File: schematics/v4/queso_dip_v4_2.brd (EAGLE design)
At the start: 41 x 50 mm, 45 parts, among them Q1 FOXSDLF/120-20, U1 PRTR5V0U2X,215, U2 PRTR5V0U2X,215, U3 PRTR5V0U2X,215, U4 PRTR5V0U2X,215, U5 PRTR5V0U2X,215, X1 USB-A-HU, X2 USB-A-HU, X3 USB-A-HU, X4 USB-A-HU

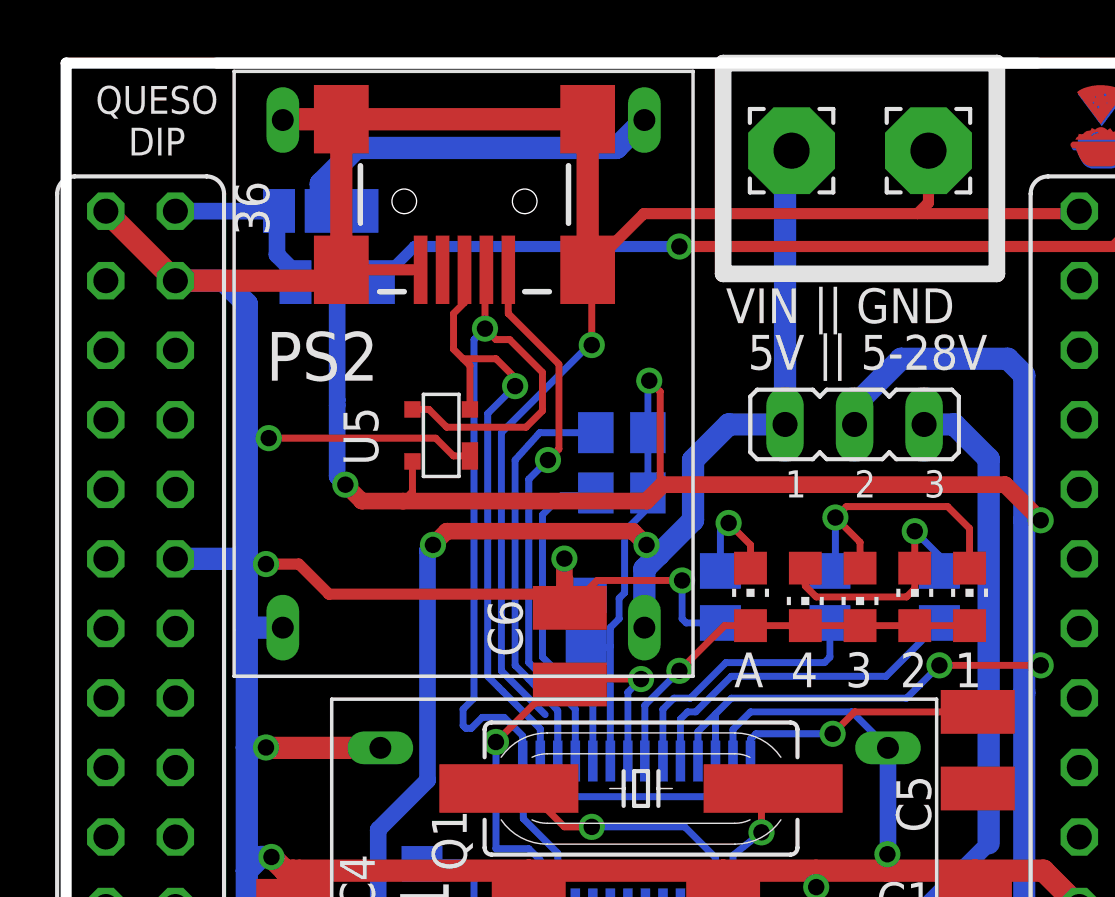
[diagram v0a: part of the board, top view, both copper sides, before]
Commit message: fixed micro usb
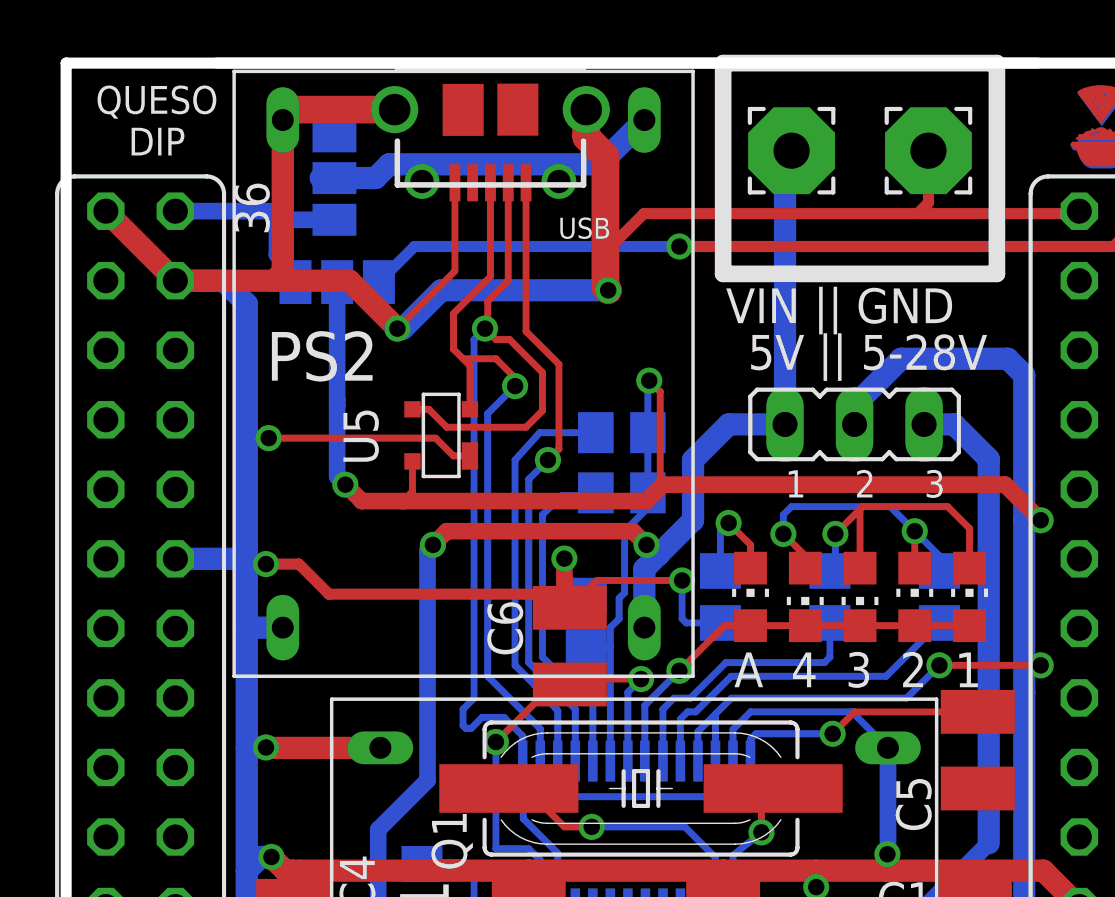
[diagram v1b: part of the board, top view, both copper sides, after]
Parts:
- removed U$8: 10118194-0001LF, SparkFun-Connectors:USB-MINIB
- added USB: USBUSB-MICROB-SMT-DIP, Spark:USB-MICROB-SMT-DIP
- moved SJ2 1.30 mm to (9.80, 45.8), turned to 90 degrees
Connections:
- net DMU: now also USB.D-; no longer U$8.D-
- net DPU: now also USB.D+; no longer U$8.D+
- net GND: now also USB.GND, USB.MT1, USB.MT2; no longer U$8.GND, U$8.MTN1, U$8.MTN2, U$8.MTN3, U$8.MTN4
- net V_UP: now also USB.VBUS; no longer U$8.VBUS
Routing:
- net GND: track 296.8 -> 288.1 mm, vias 13 -> 14
- net DMU: track 30.0 -> 33.7 mm
- net DPU: track 22.9 -> 26.5 mm
- net V_UP: track 20.6 -> 23.5 mm
- net CHR_IN: track 6.71 -> 8.75 mm
- net N$31: track 8.86 -> 10.8 mm, vias 1 -> 2
- net VOUT2: track 13.8 -> 12.7 mm
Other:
- board text added: "JKW v0.42"
- board text added: "fixed LEDs, never ordered"
- board text removed: "JKW v0.4"

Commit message: added silk logo
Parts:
- added U$4: LOGO_3X3_COPPER, logo:LOGO_3X3_COPPER
- U$2: value LOGO -> LOGO_3X3_COPPER; device logo:LOGO -> logo:LOGO_3X3_COPPER
- U$5: value LOGO -> LOGO_10X10_SILK; device logo:LOGO -> logo:LOGO_10X10_SILK
- moved U$5 37.3 mm to (5.20, 30.5), flipped to the top
- moved U$2 2.26 mm to (37.8, 47.9)
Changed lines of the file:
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@@
 1 PS (assemble PS1): C
 0 PS Passive Hub - Close D</text>
-<text x="7.3" y="38.4" size="1.778" layer="25">PS2</text>
+<text x="18" y="39.3" size="1.778" layer="25">PS2</text>
 <text x="12.2" y="20.2" size="1.778" layer="25" rot="R270">PS1</text>
 <circle x="1.45" y="44.6" radius="1.204159375" width="0.254" layer="26"/>
@@
 <text x="24.4" y="27.2" size="1.27" layer="25">A  4  3  2  1</text>
 <circle x="4" y="31.9" radius="1.204159375" width="0.254" layer="26"/>
-<text x="-3.1" y="10.7" size="1.778" layer="23" rot="R90">fixed LEDs, never ordered</text>
+<text x="-3.1" y="10.7" size="1.778" layer="19" rot="R90">fixed LEDs, never ordered</text>
 </plain>
 <attributes>
@@
 <attribute name="VALUE" x="42.979" y="0.14" size="1.27" layer="27" ratio="10" rot="R90"/>
 </element>
-<element name="U$2" library="logo" package="LOGO" value="LOGO" x="36.5379" y="46.0248"/>
-<element name="U$5" library="logo" package="LOGO" value="LOGO" x="39.0906" y="46.101" rot="MR0"/>
 <element name="U$1" library="imcom" package="FE1.1S_SSOP-28" value="FE1.1S" x="20.8393" y="21.8031" smashed="yes" rot="MR0"/>
 <element name="PAD1" library="wirepad" package="3,17/1,3" value="WIREPAD3,17/1,3" x="26.5" y="46.8" smashed="yes" rot="SR0">
@@
 <attribute name="SUPPLIER_NAME" value="Digi-Key" x="13.7" y="36.4" size="1.778" layer="27" rot="R90" display="off"/>
 <attribute name="VOLTAGE_CLAMPING" value="-" x="13.7" y="36.4" size="1.778" layer="27" rot="R90" display="off"/>
-<attribute name="NAME" x="11.4" y="35.3" size="1.27" layer="25" rot="R90"/>
+<attribute name="NAME" x="14.6" y="38.4" size="1.27" layer="25" rot="R90"/>
 </element>
 <element name="Q1" library="adafruit" package="SM49" value="FOXSDLF/120-20" x="21" y="23.5" smashed="yes">
@@
 <attribute name="VALUE" x="17.405" y="51.575" size="0.762" layer="27" rot="R180"/>
 </element>
+<element name="U$4" library="logo" package="LOGO_3X3_COPPER" value="LOGO_3X3_COPPER" x="37.8" y="47.9" rot="MR0"/>
+<element name="U$2" library="logo" package="LOGO_3X3_COPPER" value="LOGO_3X3_COPPER" x="37.8" y="47.9"/>
+<element name="U$5" library="logo" package="LOGO_10X10_SILK" value="LOGO_10X10_SILK" x="5.2" y="30.5"/>
 </elements>
 <signals>

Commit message: new logo
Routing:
- net VOUT2: track 12.7 -> 15.4 mm
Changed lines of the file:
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@@
 <contactref element="U$3" pad="VOUT"/>
 <contactref element="SJ2" pad="2"/>
-<wire x1="19.502" y1="46.3" x2="21.122" y2="47.92" width="0.8128" layer="16"/>
 <wire x1="9.3" y1="45.8" x2="9.8" y2="45.8" width="0.8128" layer="16"/>
-<wire x1="19.502" y1="46.3" x2="11.8" y2="46.3" width="0.8128" layer="16"/>
-<wire x1="11.8" y1="46.3" x2="11.3" y2="45.8" width="0.8128" layer="16"/>
 <wire x1="11.3" y1="45.8" x2="9.8" y2="45.8" width="0.8128" layer="16"/>
+<wire x1="11.3" y1="45.8" x2="11.3" y2="45.2" width="0.8128" layer="16"/>
+<wire x1="11.3" y1="45.2" x2="12.3" y2="44.2" width="0.8128" layer="16"/>
+<wire x1="12.3" y1="44.2" x2="19.1" y2="44.2" width="0.8128" layer="16"/>
+<wire x1="19.1" y1="44.2" x2="21.122" y2="46.222" width="0.8128" layer="16"/>
+<wire x1="21.122" y1="46.222" x2="21.122" y2="47.92" width="0.8128" layer="16"/>
 </signal>
 </signals>
